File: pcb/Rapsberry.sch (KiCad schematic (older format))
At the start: 6 parts, among them P1 CONN_RASPBERRY

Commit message: routing....
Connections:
- net RST_ICE: now also P1.11 (P11); no longer P1.29 (P29)
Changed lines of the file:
@@
 Text Label 3600 4550 2    50   ~ 0
 SPI_CS
-Text Label 2600 2850 0    50   ~ 0
+Text Label 2600 1950 0    50   ~ 0
 RST_ICE
 Wire Wire Line
-	2600 2850 3050 2850
+	2600 1950 3050 1950
 Text Label 3600 4650 2    50   ~ 0
 RST_ICE

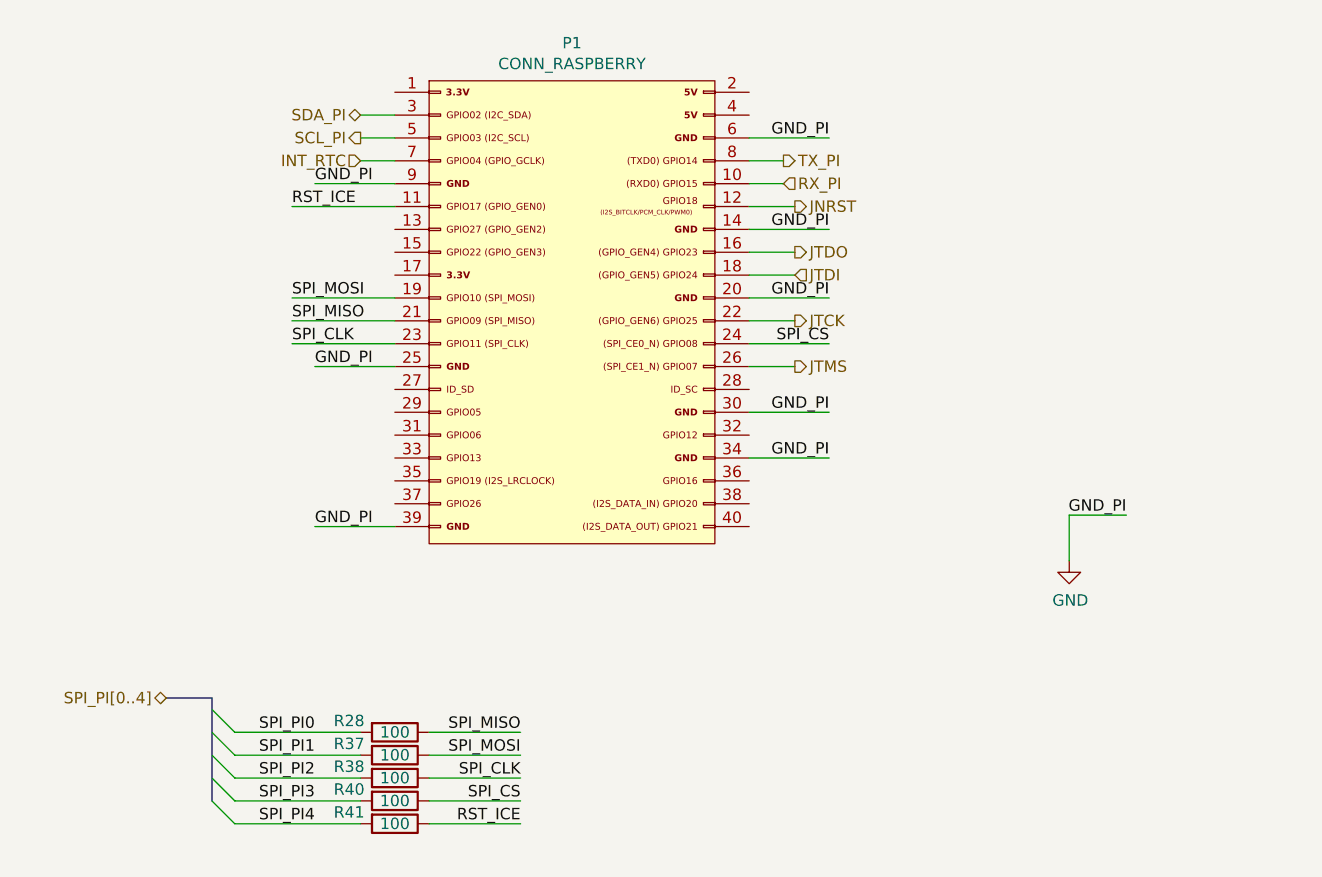
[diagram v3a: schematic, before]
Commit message: stm32 boot  modes connected to the Pi
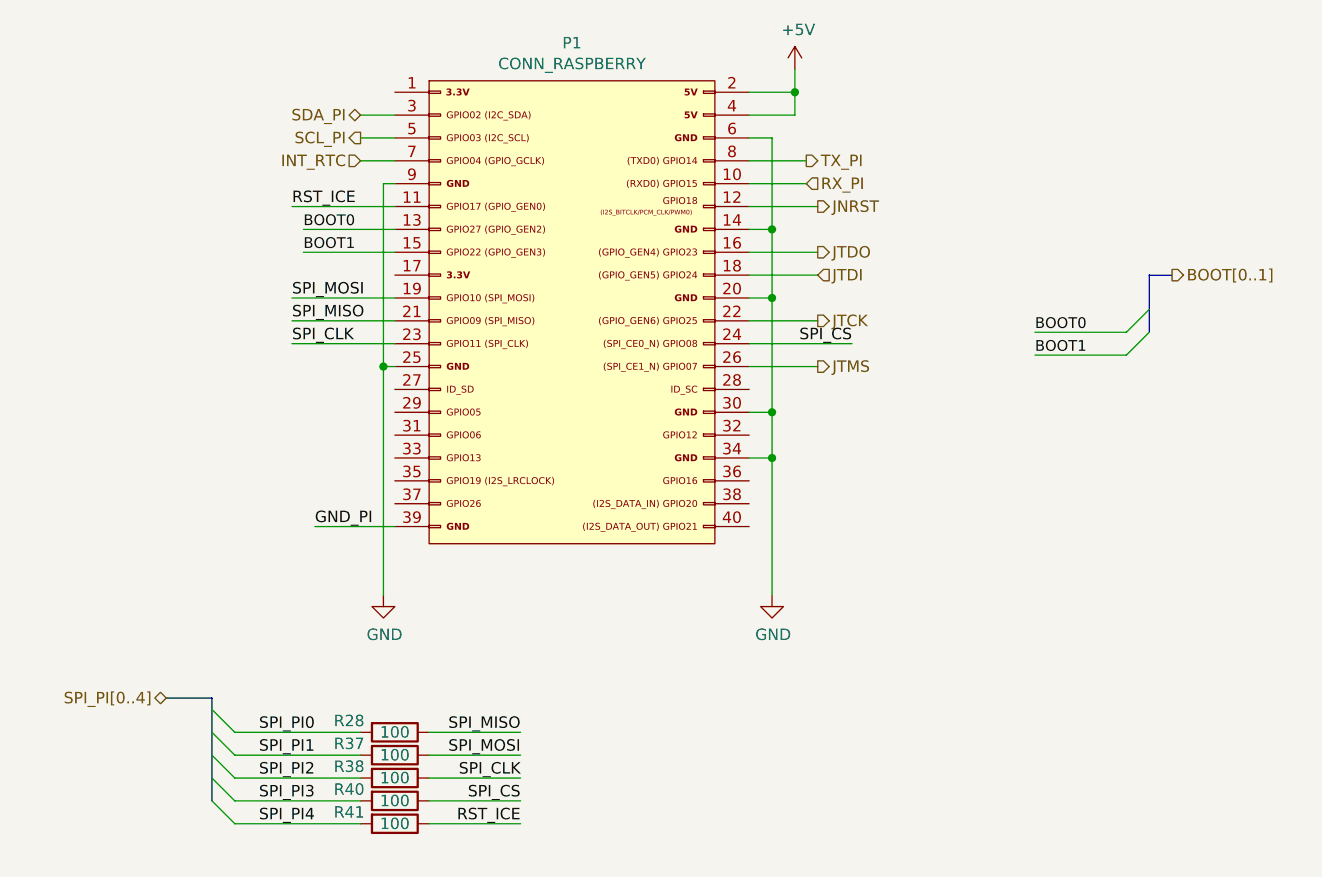
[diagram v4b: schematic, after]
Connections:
- net GND: no longer P1.39 (P39)
- net BOOT0: now reaches P1.13 (P13)
- net BOOT1: now reaches P1.15 (P15)
- net +5V: now reaches P1.2 (P2)
- net +5V: now also P1.4 (P4)
- new net GND_PI: P1.39 (P39)
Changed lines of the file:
@@
 EESchema Schematic File Version 4
+LIBS:keep_breathing_ctrl-cache
 EELAYER 30 0
 EELAYER END
@@
 $EndComp
 Wire Wire Line
-	3050 1850 2700 1850
-Text Label 2700 1850 0    50   ~ 0
-GND_PI
-Wire Wire Line
-	3050 2650 2700 2650
-Text Label 2700 2650 0    50   ~ 0
-GND_PI
-Wire Wire Line
 	3050 3350 2700 3350
 Text Label 2700 3350 0    50   ~ 0
 GND_PI
-Wire Wire Line
-	4600 3050 4950 3050
-Text Label 4950 3050 2    50   ~ 0
-GND_PI
-Wire Wire Line
-	4600 2850 4950 2850
-Text Label 4950 2850 2    50   ~ 0
-GND_PI
-Wire Wire Line
-	4600 2350 4950 2350
-Text Label 4950 2350 2    50   ~ 0
-GND_PI
-Wire Wire Line
-	4600 2050 4950 2050
-Text Label 4950 2050 2    50   ~ 0
-GND_PI
-Wire Wire Line
-	4600 1650 4950 1650
-Text Label 4950 1650 2    50   ~ 0
-GND_PI
-Text HLabel 4750 1750 2    50   Output ~ 0
+Text HLabel 4850 1750 2    50   Output ~ 0
 TX_PI
 Wire Wire Line
-	4600 1750 4750 1750
-Text HLabel 4750 1850 2    50   Input ~ 0
+	4600 1750 4850 1750
+Text HLabel 4850 1850 2    50   Input ~ 0
 RX_PI
 Wire Wire Line
-	4600 1850 4750 1850
-Wire Wire Line
-	4600 2150 4800 2150
-Wire Wire Line
-	4600 2250 4800 2250
+	4600 1850 4850 1850
+Wire Wire Line
+	4600 2150 4900 2150
+Wire Wire Line
+	4600 2250 4900 2250
 Text HLabel 2900 1550 0    50   BiDi ~ 0
 SDA_PI
@@
 L power:GND #PWR0118
 U 1 1 5E97A377
-P 6000 3500
-F 0 "#PWR0118" H 6000 3250 50  0001 C CNN
-F 1 "GND" H 6005 3327 50  0000 C CNN
-F 2 "" H 6000 3500 50  0001 C CNN
-F 3 "" H 6000 3500 50  0001 C CNN
-	1    6000 3500
+P 4700 3650
+F 0 "#PWR0118" H 4700 3400 50  0001 C CNN
+F 1 "GND" H 4705 3477 50  0000 C CNN
+F 2 "" H 4700 3650 50  0001 C CNN
+F 3 "" H 4700 3650 50  0001 C CNN
+	1    4700 3650
 	1    0    0    -1
 $EndComp
-Wire Wire Line
-	6000 3500 6000 3300
-Wire Wire Line
-	6000 3300 6250 3300
-Text Label 6250 3300 2    50   ~ 0
-GND_PI
 Text HLabel 2050 4100 0    50   BiDi ~ 0
 SPI_PI[0..4]
@@
 Text Label 2600 2550 0    50   ~ 0
 SPI_CLK
-Text Label 4950 2550 2    50   ~ 0
+Text Label 5050 2550 2    50   ~ 0
 SPI_CS
 Wire Wire Line
@@
 	2600 2550 3050 2550
 Wire Wire Line
-	4950 2550 4600 2550
+	5050 2550 4600 2550
 Text Label 3600 4250 2    50   ~ 0
 SPI_MISO
@@
 Wire Wire Line
 	3600 4650 3200 4650
-Text HLabel 4800 2650 2    50   Output ~ 0
+Text HLabel 4900 2650 2    50   Output ~ 0
 JTMS
-Text HLabel 4800 2450 2    50   Output ~ 0
+Text HLabel 4900 2450 2    50   Output ~ 0
 JTCK
-Text HLabel 4800 2250 2    50   Input ~ 0
+Text HLabel 4900 2250 2    50   Input ~ 0
 JTDI
-Text HLabel 4800 2150 2    50   Output ~ 0
+Text HLabel 4900 2150 2    50   Output ~ 0
 JTDO
 Wire Wire Line
-	4800 2450 4600 2450
-Wire Wire Line
-	4800 2650 4600 2650
-Wire Wire Line
-	4800 1950 4600 1950
-Text HLabel 4800 1950 2    50   Output ~ 0
+	4900 2450 4600 2450
+Wire Wire Line
+	4900 2650 4600 2650
+Wire Wire Line
+	4900 1950 4600 1950
+Text HLabel 4900 1950 2    50   Output ~ 0
 JNRST
+Text Label 5850 2500 0    47   ~ 0
+BOOT0
+Text Label 5850 2600 0    47   ~ 0
+BOOT1
+Wire Bus Line
+	6350 2250 6450 2250
+Text HLabel 6450 2250 2    50   Output ~ 0
+BOOT[0..1]
+Entry Wire Line
+	6250 2500 6350 2400
+Entry Wire Line
+	6250 2600 6350 2500
+Wire Wire Line
+	5850 2500 6250 2500
+Wire Wire Line
+	5850 2600 6250 2600
+Text Label 2650 2050 0    47   ~ 0
+BOOT0
+Text Label 2650 2150 0    47   ~ 0
+BOOT1
+Wire Wire Line
+	2650 2050 3050 2050
+Wire Wire Line
+	2650 2150 3050 2150
+$Comp
+L power:+5V #PWR0130
+U 1 1 5ECDCFFC
+P 4800 1350
+F 0 "#PWR0130" H 4800 1200 50  0001 C CNN
+F 1 "+5V" H 4815 1523 50  0000 C CNN
+F 2 "" H 4800 1350 50  0001 C CNN
+F 3 "" H 4800 1350 50  0001 C CNN
+	1    4800 1350
+	1    0    0    -1
+$EndComp
+Wire Wire Line
+	4800 1350 4800 1450
+Wire Wire Line
+	4800 1550 4600 1550
+Wire Wire Line
+	4600 1450 4800 1450
+Connection ~ 4800 1450
+Wire Wire Line
+	4800 1450 4800 1550
+Wire Wire Line
+	4600 1650 4700 1650
+Wire Wire Line
+	4700 1650 4700 2050
+Wire Wire Line
+	4600 3050 4700 3050
+Connection ~ 4700 3050
+Wire Wire Line
+	4700 3050 4700 3650
+Wire Wire Line
+	4600 2850 4700 2850
+Connection ~ 4700 2850
+Wire Wire Line
+	4700 2850 4700 3050
+Wire Wire Line
+	4600 2350 4700 2350
+Connection ~ 4700 2350
+Wire Wire Line
+	4700 2350 4700 2850
+Wire Wire Line
+	4600 2050 4700 2050
+Connection ~ 4700 2050
+Wire Wire Line
+	4700 2050 4700 2350
+$Comp
+L power:GND #PWR0151
+U 1 1 5ECF1E11
+P 3000 3650
+F 0 "#PWR0151" H 3000 3400 50  0001 C CNN
+F 1 "GND" H 3005 3477 50  0000 C CNN
+F 2 "" H 3000 3650 50  0001 C CNN
+F 3 "" H 3000 3650 50  0001 C CNN
+	1    3000 3650
+	1    0    0    -1
+$EndComp
+Wire Wire Line
+	3050 1850 3000 1850
+Wire Wire Line
+	3000 1850 3000 2650
+Wire Wire Line
+	3050 2650 3000 2650
+Wire Bus Line
+	6350 2250 6350 2500
 Wire Bus Line
 	2250 4100 2250 4550
+Connection ~ 3000 2650
+Wire Wire Line
+	3000 2650 3000 3650
 $EndSCHEMATC

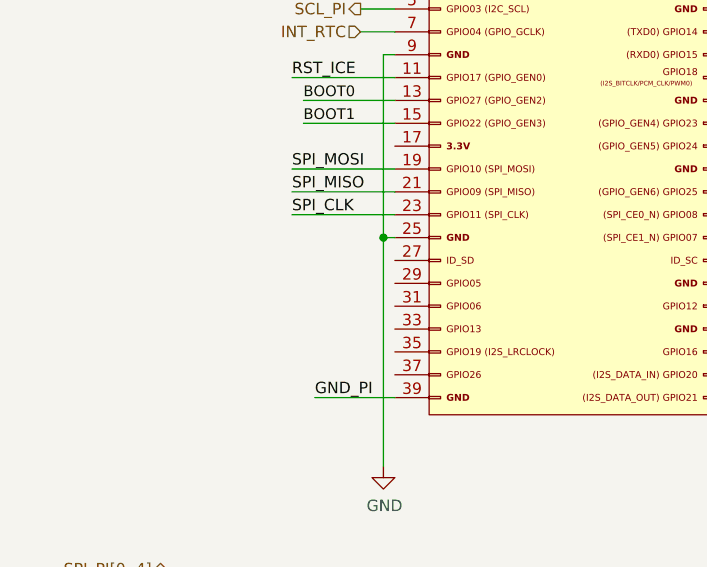
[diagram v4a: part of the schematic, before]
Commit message: relay VCC fixed
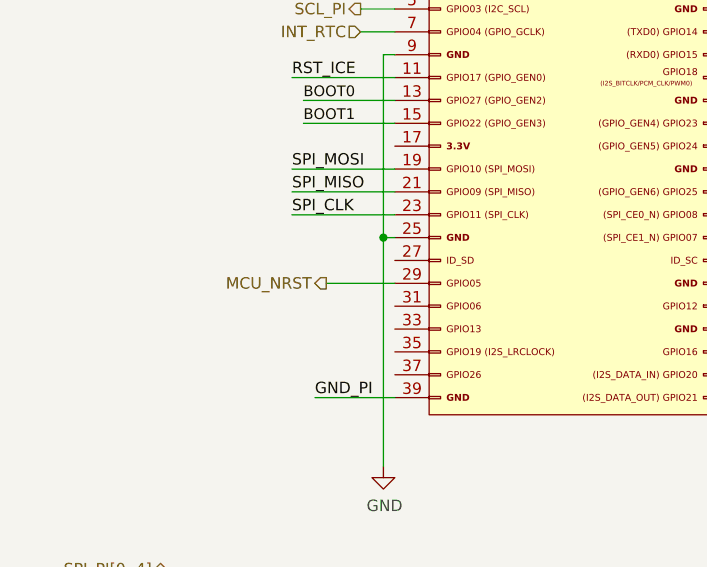
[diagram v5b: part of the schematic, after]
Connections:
- net MCU_NRST: now reaches P1.29 (P29)
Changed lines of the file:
@@
 Wire Wire Line
 	3050 2650 3000 2650
+Connection ~ 3000 2650
+Wire Wire Line
+	3000 2650 3000 3650
+Wire Wire Line
+	2750 2850 3050 2850
+Text HLabel 2750 2850 0    50   Output ~ 0
+MCU_NRST
 Wire Bus Line
 	6350 2250 6350 2500
 Wire Bus Line
 	2250 4100 2250 4550
-Connection ~ 3000 2650
-Wire Wire Line
-	3000 2650 3000 3650
 $EndSCHEMATC

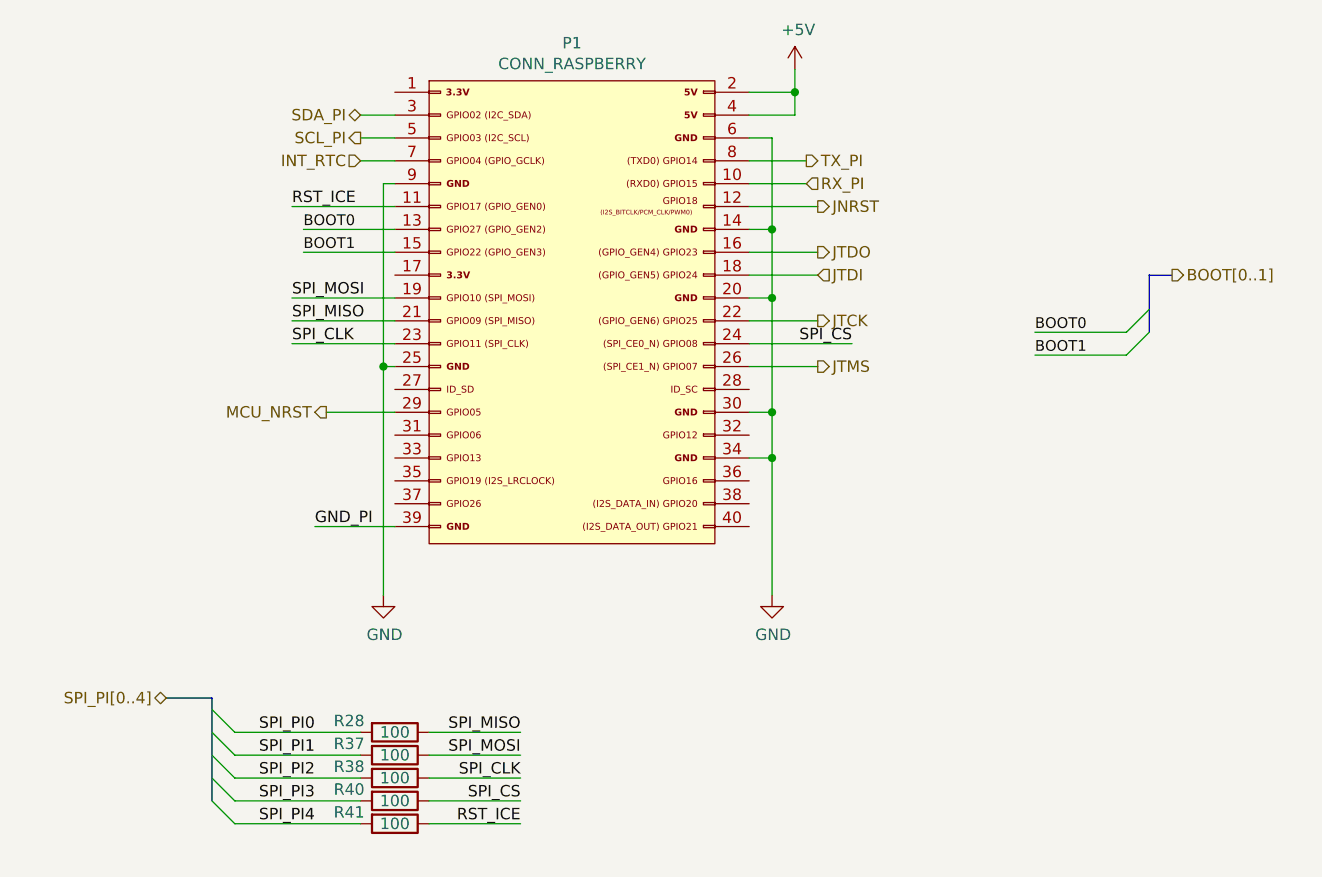
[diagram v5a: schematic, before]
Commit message: 2 CS for FPGA
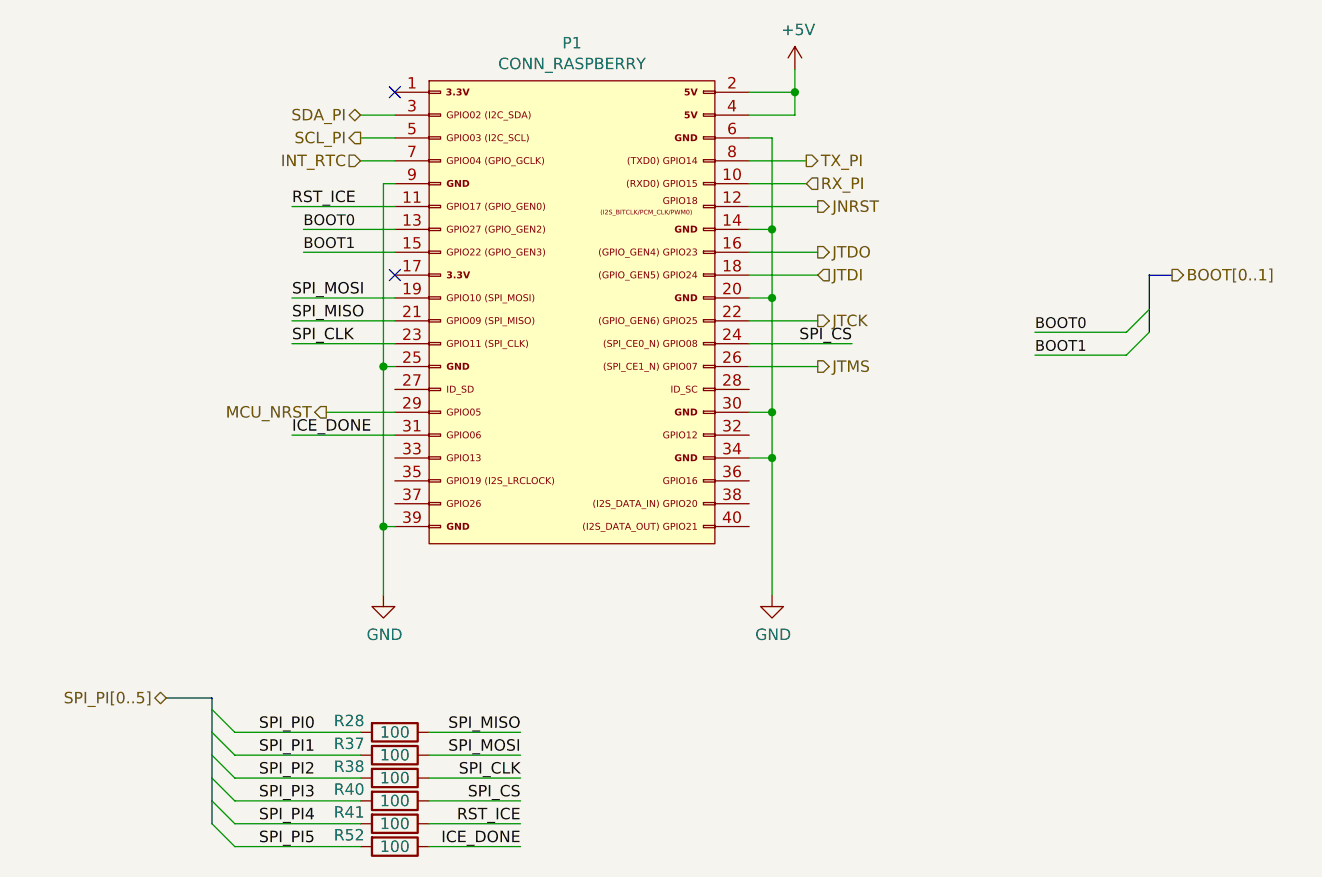
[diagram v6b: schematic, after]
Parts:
- added R52: 100, Resistor_SMD:R_0402_1005Metric, symbol Device:R
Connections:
- net GND_PI is gone; now on net GND: P1.39 (P39)
- net ICE_DONE: now reaches P1.31 (P31)
- net ICE_DONE: now also R52.1
- new net SPI_PI5: R52.2
- no-connect marks 0 -> 2
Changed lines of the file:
@@
 	1    0    0    -1
 $EndComp
-Wire Wire Line
-	3050 3350 2700 3350
-Text Label 2700 3350 0    50   ~ 0
-GND_PI
 Text HLabel 4850 1750 2    50   Output ~ 0
 TX_PI
@@
 $EndComp
 Text HLabel 2050 4100 0    50   BiDi ~ 0
-SPI_PI[0..4]
+SPI_PI[0..5]
 Wire Bus Line
 	2050 4100 2250 4100
@@
 Connection ~ 3000 2650
 Wire Wire Line
-	3000 2650 3000 3650
+	3000 2650 3000 3350
 Wire Wire Line
 	2750 2850 3050 2850
 Text HLabel 2750 2850 0    50   Output ~ 0
 MCU_NRST
+Entry Wire Line
+	2250 4650 2350 4750
+Text Label 2700 4750 2    50   ~ 0
+SPI_PI5
+Text Label 3600 4750 2    50   ~ 0
+ICE_DONE
+Wire Wire Line
+	2350 4750 2900 4750
+$Comp
+L Device:R R52
+U 1 1 5F0CC2C5
+P 3050 4750
+F 0 "R52" V 3000 4550 50  0000 C CNN
+F 1 "100" V 3050 4750 50  0000 C CNN
+F 2 "Resistor_SMD:R_0402_1005Metric" V 2980 4750 50  0001 C CNN
+F 3 "~" H 3050 4750 50  0001 C CNN
+	1    3050 4750
+	0    1    1    0
+$EndComp
+Wire Wire Line
+	3600 4750 3200 4750
+Text Label 2600 2950 0    50   ~ 0
+ICE_DONE
+Wire Wire Line
+	2600 2950 3050 2950
+Wire Wire Line
+	3050 3350 3000 3350
+Connection ~ 3000 3350
+Wire Wire Line
+	3000 3350 3000 3650
+NoConn ~ 3050 1450
+NoConn ~ 3050 2250
 Wire Bus Line
 	6350 2250 6350 2500
 Wire Bus Line
-	2250 4100 2250 4550
+	2250 4100 2250 4650
 $EndSCHEMATC

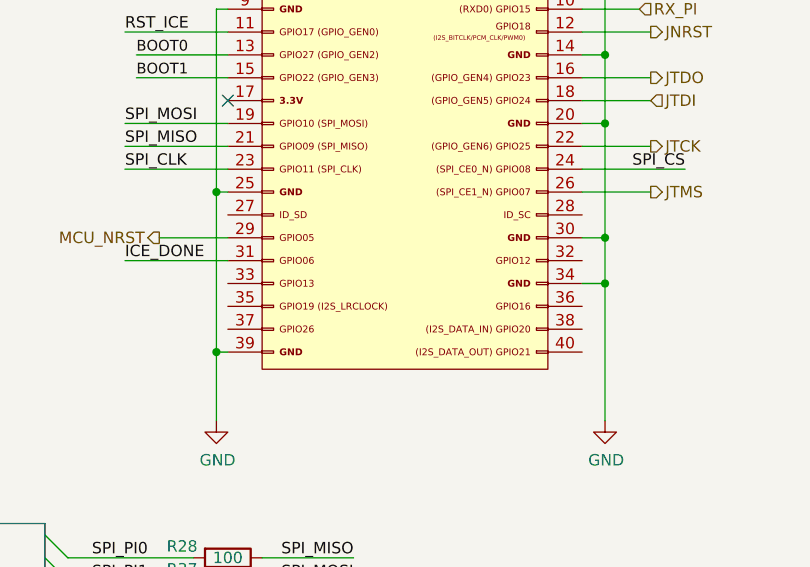
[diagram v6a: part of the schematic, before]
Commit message: Solved connections showed wrong by ERC
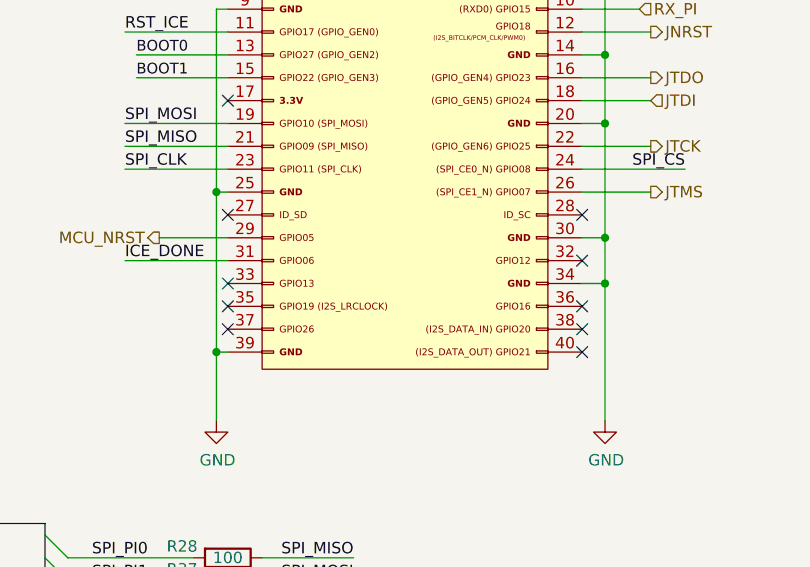
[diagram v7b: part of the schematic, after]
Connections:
- no-connect marks 2 -> 11
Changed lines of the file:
@@
 EESchema Schematic File Version 4
-LIBS:keep_breathing_ctrl-cache
 EELAYER 30 0
 EELAYER END
@@
 NoConn ~ 3050 1450
 NoConn ~ 3050 2250
+NoConn ~ 3050 2750
+NoConn ~ 3050 3050
+NoConn ~ 3050 3150
+NoConn ~ 3050 3250
+NoConn ~ 4600 2750
+NoConn ~ 4600 2950
+NoConn ~ 4600 3150
+NoConn ~ 4600 3250
+NoConn ~ 4600 3350
 Wire Bus Line
 	6350 2250 6350 2500

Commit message: Added components dikey part numbers in modified sheets
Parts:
- P1: DigiKey (none) -> S5690-ND
- R28, R37, R38, R40, R41, R52: DigiKey (none) -> P100LCT-ND
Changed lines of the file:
@@
 F 2 "SMD:SMD_CONN_2x20" H 3825 3481 60  0001 C CNN
 F 3 "" H 3300 1450 60  0000 C CNN
+F 4 "S5690-ND" H 4100 2400 50  0001 C CNN "DigiKey"
 	1    4100 2400
 	1    0    0    -1
@@
 F 2 "Resistor_SMD:R_0402_1005Metric" V 2980 4250 50  0001 C CNN
 F 3 "~" H 3050 4250 50  0001 C CNN
+F 4 "P100LCT-ND" V 3050 4250 50  0001 C CNN "DigiKey"
 	1    3050 4250
 	0    1    1    0
@@
 F 2 "Resistor_SMD:R_0402_1005Metric" V 2980 4350 50  0001 C CNN
 F 3 "~" H 3050 4350 50  0001 C CNN
+F 4 "P100LCT-ND" V 3050 4350 50  0001 C CNN "DigiKey"
 	1    3050 4350
 	0    1    1    0
@@
 F 2 "Resistor_SMD:R_0402_1005Metric" V 2980 4450 50  0001 C CNN
 F 3 "~" H 3050 4450 50  0001 C CNN
+F 4 "P100LCT-ND" V 3050 4450 50  0001 C CNN "DigiKey"
 	1    3050 4450
 	0    1    1    0
@@
 F 2 "Resistor_SMD:R_0402_1005Metric" V 2980 4550 50  0001 C CNN
 F 3 "~" H 3050 4550 50  0001 C CNN
+F 4 "P100LCT-ND" V 3050 4550 50  0001 C CNN "DigiKey"
 	1    3050 4550
 	0    1    1    0
@@
 F 2 "Resistor_SMD:R_0402_1005Metric" V 2980 4650 50  0001 C CNN
 F 3 "~" H 3050 4650 50  0001 C CNN
+F 4 "P100LCT-ND" V 3050 4650 50  0001 C CNN "DigiKey"
 	1    3050 4650
 	0    1    1    0
@@
 F 2 "Resistor_SMD:R_0402_1005Metric" V 2980 4750 50  0001 C CNN
 F 3 "~" H 3050 4750 50  0001 C CNN
+F 4 "P100LCT-ND" V 3050 4750 50  0001 C CNN "DigiKey"
 	1    3050 4750
 	0    1    1    0
